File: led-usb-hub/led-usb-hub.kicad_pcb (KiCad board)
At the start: 4 copper layers, 127 x 50.8 mm, 144 parts, among them J1 USBC_USB2.0, J2 RGBUSB_54-00266, J3 RGBUSB_54-00266, J4 RGBUSB_54-00266, J5 SWD, SW1 RESET, SW2 BOOLSEL, SW3 LED_EN, U1 RP2040, U10 TPD2EUSB30, U11 TPD2EUSB30, U12 TC54VN3002, U13 W25Q16JVSN, U2 TPS2042D, U3 TPS2042D, U4 TPS563257DRLR, U5 TPS563257DRLR, U6 TUSB2046IBVF, U7 TPD2EUSB30, U8 TPD2EUSB30, U9 TPD2EUSB30, Y1 12Mhz, Y2 6Mhz

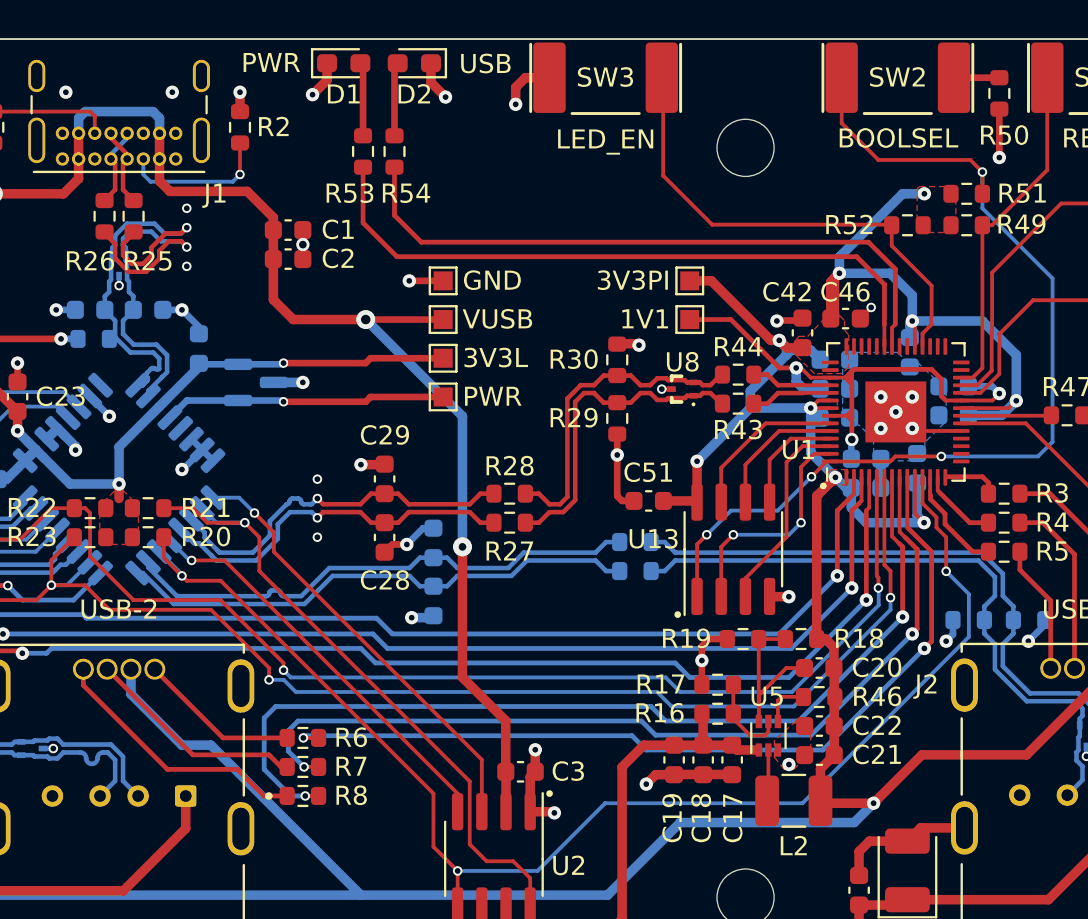
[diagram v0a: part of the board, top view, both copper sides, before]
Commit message: Clean up, label all nets
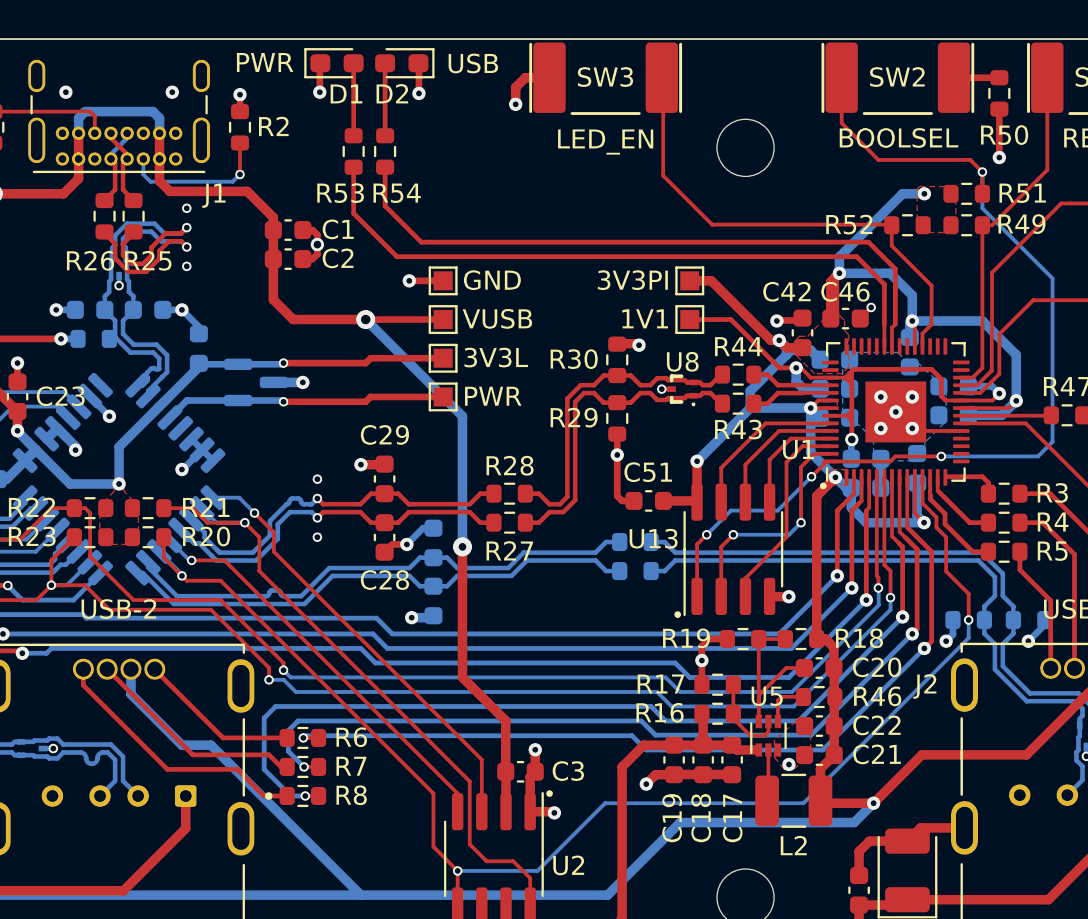
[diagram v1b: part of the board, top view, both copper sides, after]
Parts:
- moved D2 0.66 mm to (111.9, 83.1)
- moved R53 0.49 mm to (109.3, 87.7)
- moved R54 0.49 mm to (111.0, 87.7)
- moved D1 0.35 mm to (108.5, 83.1)
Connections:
- net Net-(C48-Pad1) renamed /OSC_PI2
- net Net-(C50-Pad1) renamed /OSC_USB2
- net Net-(J1-CC1) renamed /CC1
- net Net-(J1-CC2) renamed /CC2
- net Net-(R50-Pad2) renamed /BOOTSEL'
- net Net-(U1-GPIO21) renamed /EN_LED
- net Net-(U1-XIN) renamed /OSC_PI1
- net Net-(U1-XOUT) renamed /OSC_PI2'
- net Net-(U4-EN) renamed /EN_REG_L
- net Net-(U4-FB) renamed /FB_REG_L
- net Net-(U4-PG) renamed /PG_REG_L
- net Net-(U4-SW) renamed /SW_REG_L
- net Net-(U5-EN) renamed /EN_REG_PI
- net Net-(U5-FB) renamed /FB_REG_PI
- net Net-(U5-PG) renamed /PG_REG_PI
- net Net-(U5-SW) renamed /SW_REG_PI
- net Net-(U6-XTAL1) renamed /OSC_USB1
- net Net-(U6-XTAL2) renamed /OSC_USB2'
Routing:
- net Earth: track 126.7 -> 128.4 mm
- net +3V3_L: track 56.6 -> 55.9 mm

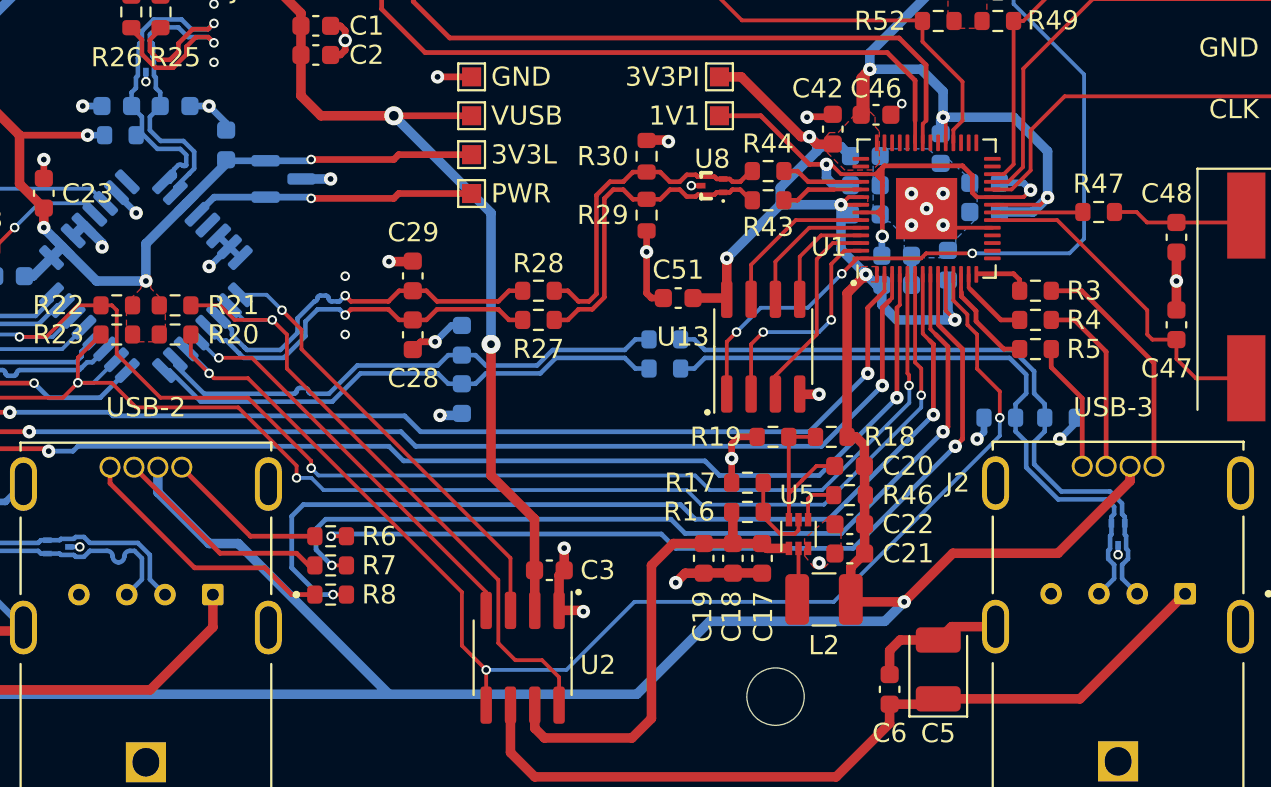
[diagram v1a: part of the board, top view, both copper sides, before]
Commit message: More clean up, better pin assignment for decoupling
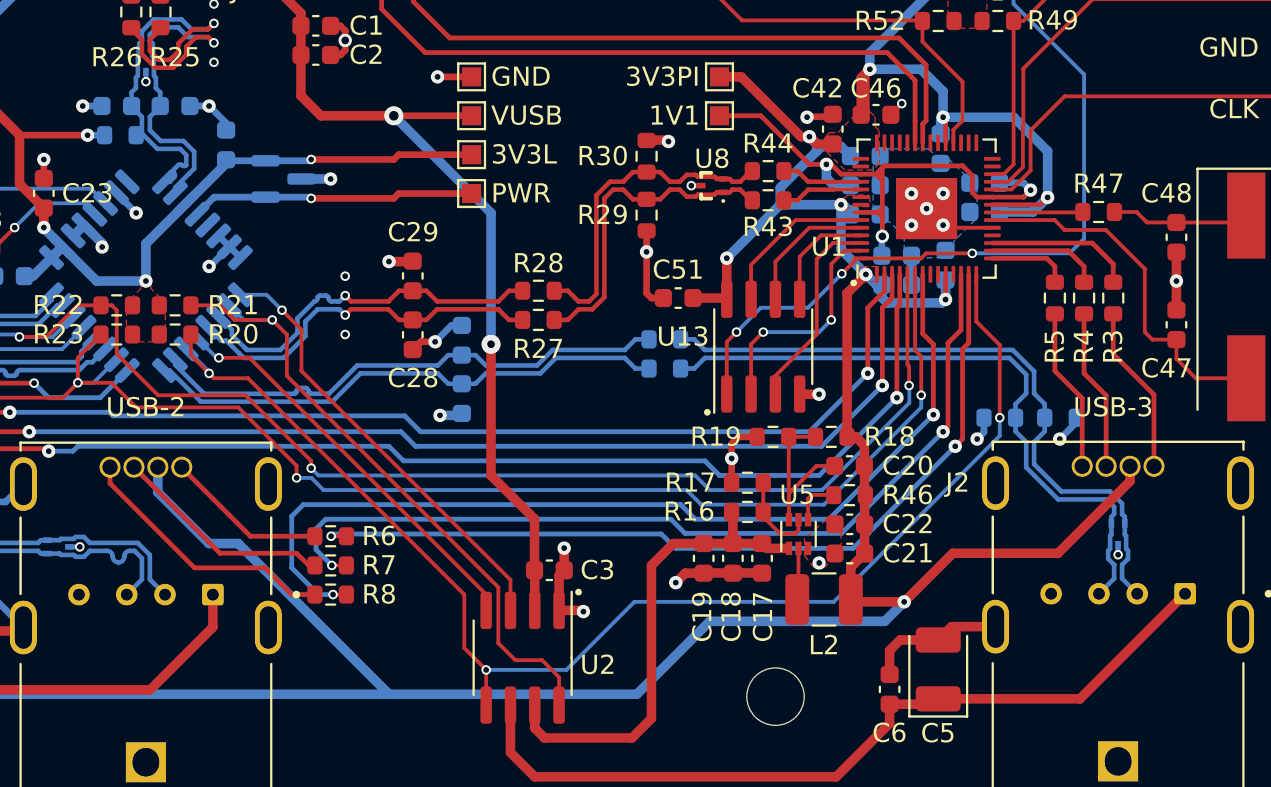
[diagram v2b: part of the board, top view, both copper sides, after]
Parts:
- moved R3 4.08 mm to (147.6, 106.0), turned to -90 degrees
- moved R5 2.85 mm to (144.5, 106.0), turned to -90 degrees
- moved R4 2.79 mm to (146.1, 106.0), turned to -90 degrees
- moved C44 0.13 mm to (138.8, 104.3)
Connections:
- U1 pad 11: OC1 -> unconnected-(U1-GPIO8-Pad11)
- U1 pad 12: L1_B -> L2_G
- U1 pad 13: L1_G -> L2_R
- U1 pad 14: L1_R -> OC1
- U1 pad 15: unconnected-(U1-GPIO12-Pad15) -> L1_B
- U1 pad 16: unconnected-(U1-GPIO13-Pad16) -> L1_G
- U1 pad 17: unconnected-(U1-GPIO14-Pad17) -> L1_R
- U1 pad 8: L2_G -> unconnected-(U1-GPIO6-Pad8)
- U1 pad 9: L2_R -> unconnected-(U1-GPIO7-Pad9)
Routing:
- net +3V3_PI: track 229.9 -> 223.5 mm
- net L1_R: track 2.92 -> 7.72 mm
- net /L1_R': track 12.3 -> 8.85 mm
- net L1_G: track 4.06 -> 5.96 mm
- net /L1_B': track 6.79 -> 8.56 mm
- net L1_B: track 5.65 -> 4.27 mm
- net /OSC_PI1: track 18.0 -> 19.2 mm
- net /L1_G': track 9.54 -> 8.44 mm
- added copper zone on B.Cu, net +3V3_PI

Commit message: Even more goddamn clean up and closer placement of decoupling caps
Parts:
- moved C43 0.41 mm to (138.8, 98.6)
- moved C38 0.23 mm to (141.1, 100.0)
- moved C41 0.23 mm to (141.1, 101.5)
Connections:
- U1 pad 31: unconnected-(U1-GPIO20-Pad31) -> /EN_LED
- U1 pad 32: /EN_LED -> unconnected-(U1-GPIO21-Pad32)
- U1 pad 35: unconnected-(U1-GPIO23-Pad35) -> LED_USB
- U1 pad 36: LED_USB -> LED_PWR
- U1 pad 37: LED_PWR -> unconnected-(U1-GPIO25-Pad37)
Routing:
- net +3V3_PI: track 223.5 -> 221.1 mm, vias 11 -> 12
- net +5V_1: track 42.4 -> 43.8 mm
- net Earth: track 128.4 -> 127.5 mm
- net PWR_EN1: track 21.5 -> 20.7 mm
- net +5V_2: track 27.1 -> 27.8 mm
- net /L2_R': track 8.44 -> 9.03 mm
- net /L2_G': track 11.6 -> 12.1 mm

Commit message: Clean up and aligning
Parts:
- D1: value ORANGE (PWR) -> PWR
- D2: value GREEN (USB) -> USB
- SW3: value LED_EN -> LED EN
- moved C4 1.66 mm to (79.1, 120.1)
- moved U3 1.65 mm to (77.9, 124.7)
- moved C25 0.73 mm to (100.8, 98.7)
- moved C3 0.18 mm to (118.0, 120.1)
- moved U2 0.13 mm to (116.7, 124.7)
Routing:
- net Earth: track 127.5 -> 125.6 mm, vias 61 -> 62
- net +5V_3: track 33.4 -> 31.7 mm
- net VUSB: track 138.1 -> 136.4 mm
- net +5V_2: track 27.8 -> 29.3 mm
- net OC1: track 69.4 -> 70.4 mm
- net OC3: track 94.0 -> 95.0 mm
- net PWR_EN1: track 20.7 -> 21.5 mm
- net PWR_EN2: track 27.6 -> 28.3 mm
- net PWR_EN3: track 26.6 -> 27.2 mm
- net OC2: track 89.0 -> 89.7 mm
- net +5V_1: track 43.8 -> 43.3 mm

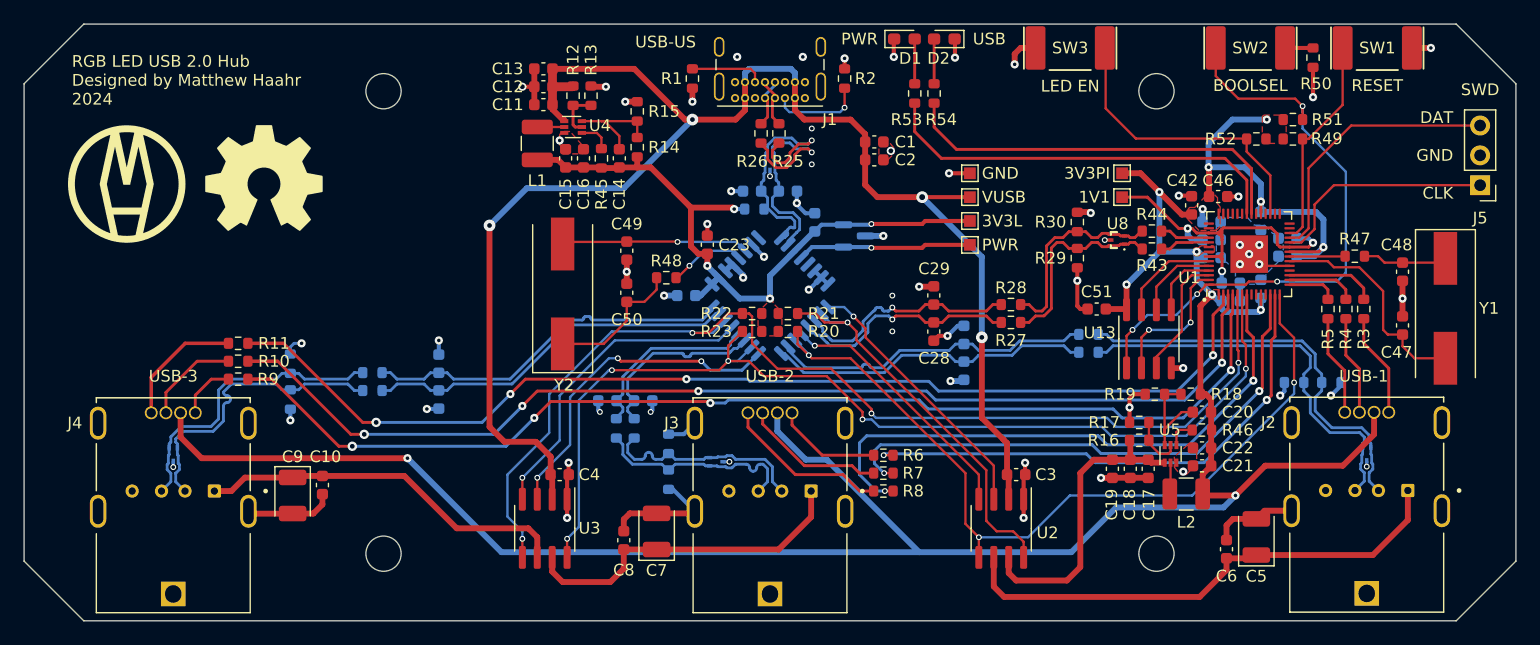
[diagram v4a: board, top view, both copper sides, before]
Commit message: Correct Annular Ring Sizes
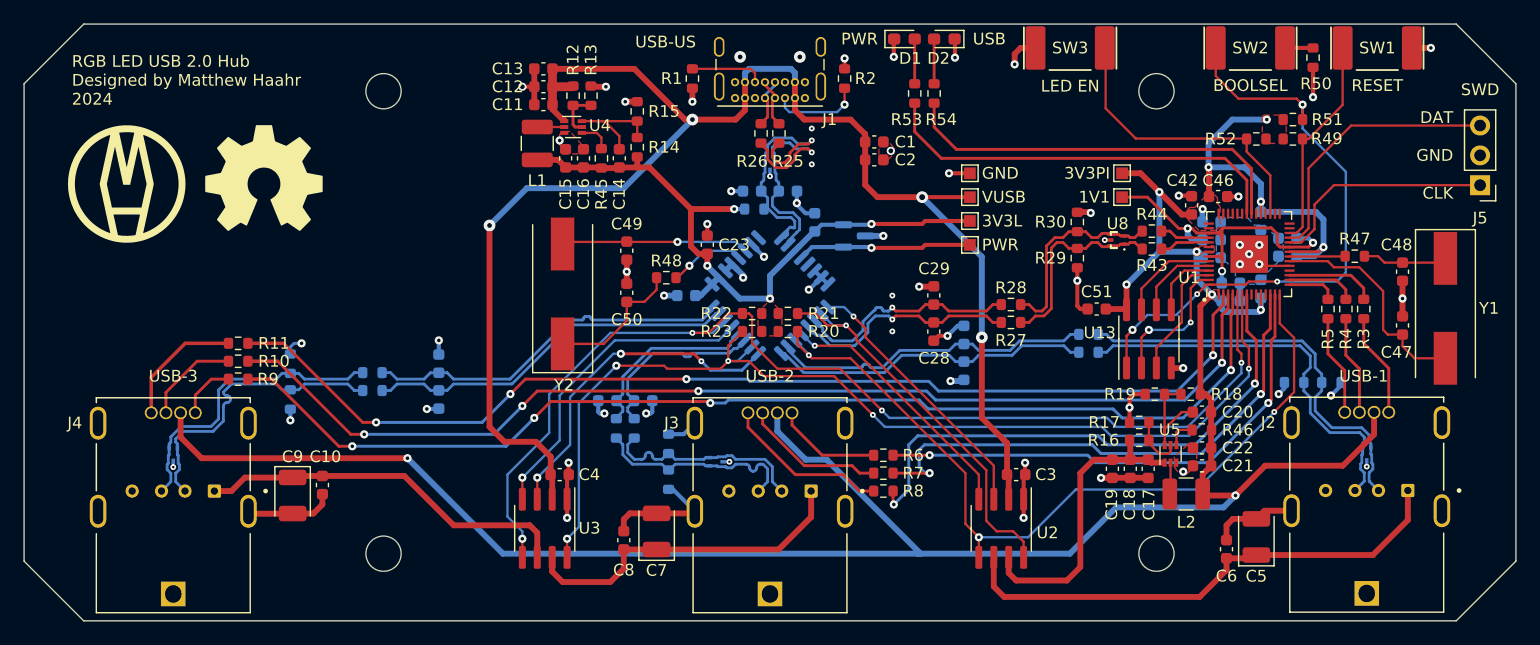
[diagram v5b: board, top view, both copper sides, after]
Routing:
- net L2_B: track 50.1 -> 47.1 mm
- net L2_R: track 45.3 -> 43.8 mm
- net Earth: track 125.6 -> 127.0 mm
- net L2_G: track 47.1 -> 46.2 mm
- net +3V3_PI: track 221.1 -> 221.7 mm

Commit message: Larger inductor traces
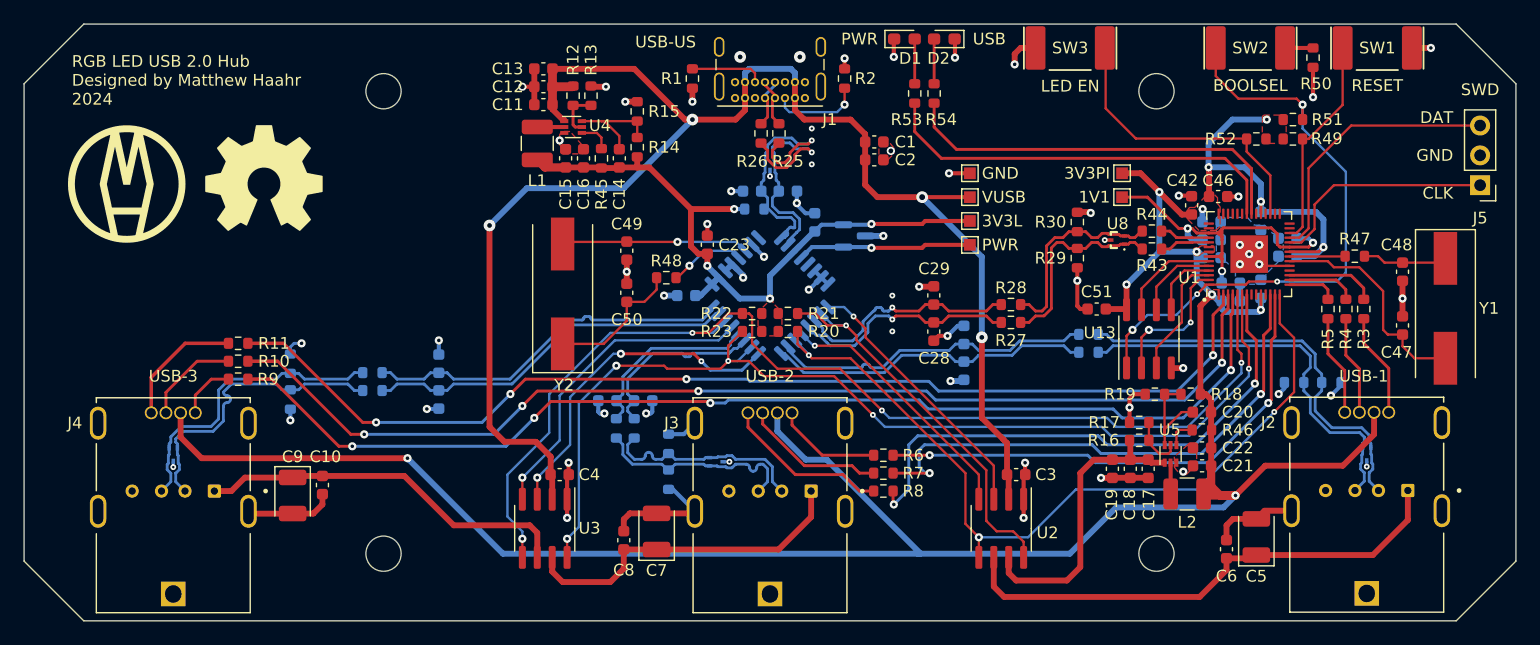
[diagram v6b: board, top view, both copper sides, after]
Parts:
- moved L2 0.08 mm to (132.5, 121.8)
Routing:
- net +3V3_PI: track 221.7 -> 226.8 mm
- net /SW_REG_PI: track 2.60 -> 5.27 mm

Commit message: More zoning
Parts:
- moved C11 0.13 mm to (77.9, 88.6)
- moved C12 0.13 mm to (77.9, 87.1)
- moved C13 0.13 mm to (77.9, 85.6)
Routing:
- net Earth: track 127.0 -> 113.9 mm
- net VUSB: track 136.4 -> 125.2 mm, vias 4 -> 2
- net +5V_0: track 25.2 -> 19.1 mm
- added copper zone on F.Cu, net +5V_0
- added copper zone on F.Cu, net VUSB

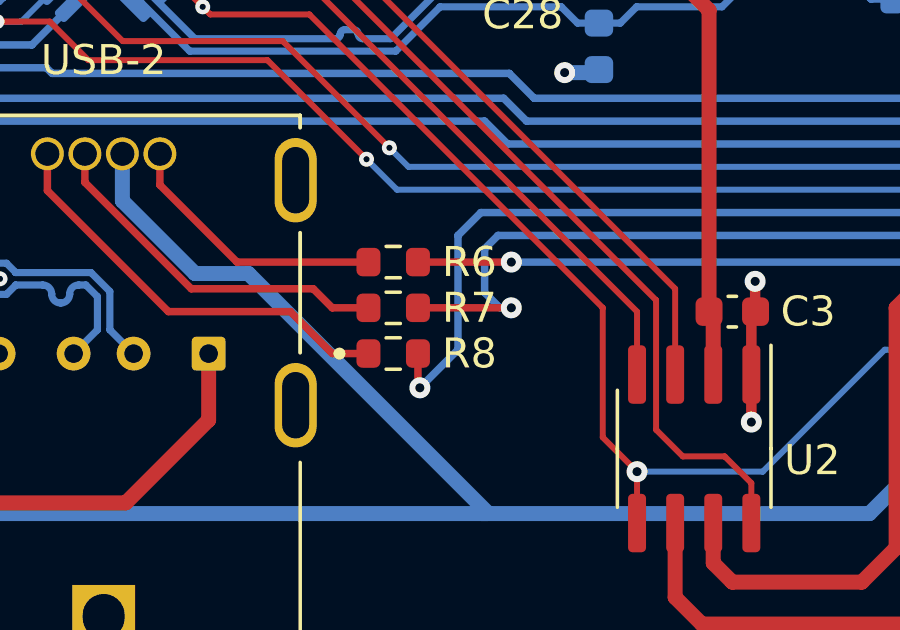
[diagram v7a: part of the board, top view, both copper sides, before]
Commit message: Pick better LED resistor values
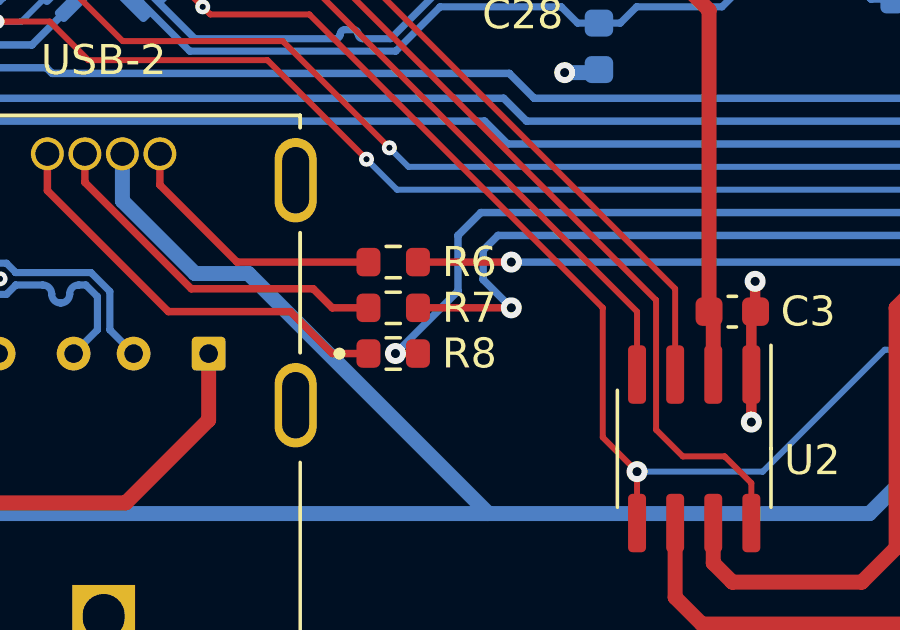
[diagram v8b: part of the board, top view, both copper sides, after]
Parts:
- R10, R4, R7: value 30 -> 62
- R11, R5, R8: value 30 -> 27
- R3, R6, R9: value 130 -> 200
- R53: value 300 -> 2k
- R54: value 300 -> 2.4k
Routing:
- net L2_B: track 47.1 -> 45.9 mm
